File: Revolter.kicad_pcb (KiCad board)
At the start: 2 copper layers, 100 x 100 mm, 179 parts, among them IC1 LM5017, IC2 AP65111, IC3 INA181A1, IC4 INA181A1, P1 USB_OTG, P10 AUX, P2 CAN, P3 IN+, P4 IN-, P5 MOTOR3, P6 MOTOR2, P7 MOTOR1, P8 SWD, P9 Motor, Q1 ZXTC2045E6, Q10 ZXTC2045E6, Q13 IRFB4110, Q14 IRFB4110, Q15 IRFB4110, Q16 IRFB4110, Q19 IRFB4110, Q2 ZXTC2045E6, Q20 IRFB4110, Q21 IRFB4110, Q22 IRFB4110, Q3 IRFB4110, Q4 IRFB4110, Q5 ZXTC2045E6, Q6 ZXTC2045E6, Q7 IRFB4110, Q8 IRFB4110, Q9 ZXTC2045E6, U1 STM32F40X_LQFP64, U2 IR2110S, U3 IR2110S, U4 IR2110S, U5 PCA82C251, U6 7805_SO8, X1 8MHz 10ppm

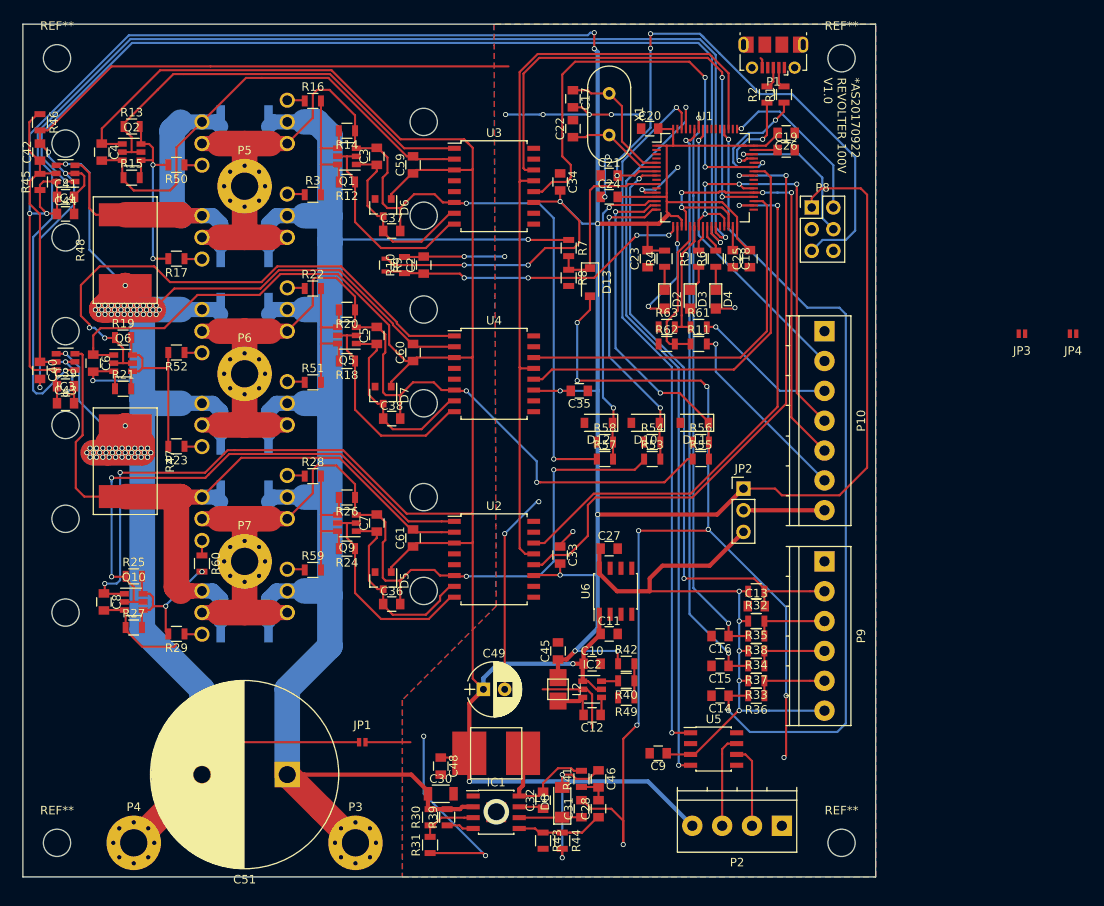
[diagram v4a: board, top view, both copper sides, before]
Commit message: - basis commit for V1.1 - did an great overhaul of high current paths - fixed wrong 3V3 reg pin out - blew the IO connector up to 8 pins (turns out 7pin is rare) - changed shunt to 2512 - changed hf caps to double 1210 - two input caps - pin outs for all IO on silk screen - spread the references so you can actually read them - connected the Hall/Temp pull-ups to 3V3 instead of 5V - changed vias to 0.6/0.3mm - changed text to V1.1
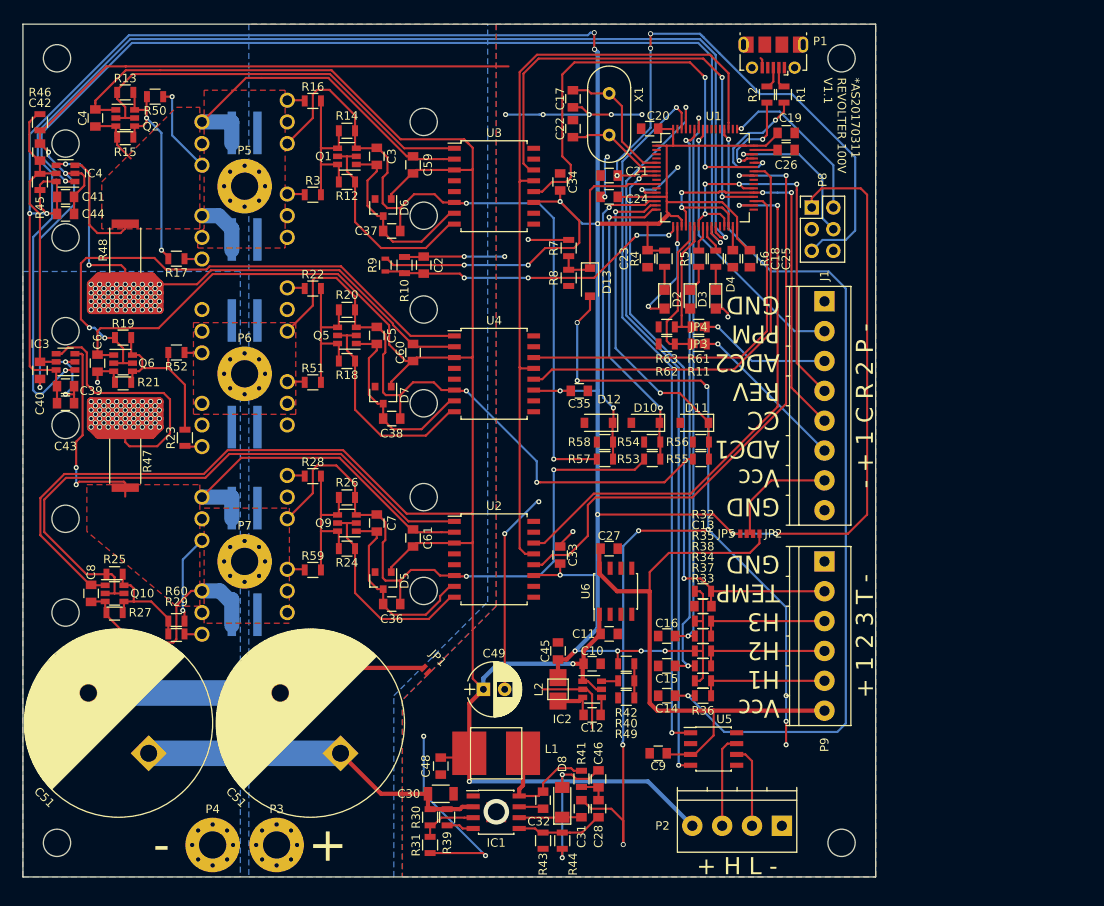
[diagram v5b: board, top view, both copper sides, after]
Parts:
- removed P10: AUX, Connectors_Terminal_Blocks:TerminalBlock_Pheonix_PT-3.5mm_7pol
- added C1: 2u2 250V, Capacitors_SMD:C_1210, B.Cu at (85.0, 65.0)
- added C29: 2u2 250V, Capacitors_SMD:C_1210, B.Cu at (85.0, 55.0)
- added C47: 2u2 250V, Capacitors_SMD:C_1210, B.Cu at (85.0, 87.0)
- added C50: 2u2 250V, Capacitors_SMD:C_1210, B.Cu at (85.0, 77.0)
- added C51: 1mF 100V, alexmod:C_Radial_D22_P10, F.Cu at (73.8, 126.5)
- added C53: 2u2 250V, Capacitors_SMD:C_1210, B.Cu at (85.0, 99.0)
- added C62: 2u2 250V, Capacitors_SMD:C_1210, B.Cu at (85.0, 109.0)
- added J1: IO, Connectors_Terminal_Blocks:TerminalBlock_Pheonix_PT-3.5mm_8pol, F.Cu at (153.0, 73.5)
- added JP5: opt., alexmod:Jumper_2, F.Cu at (143.5, 100.8)
- C52, C54, C55, C56, C57, C58: footprint Capacitors_SMD:C_2220 -> Capacitors_SMD:C_1210
- JP2: value Vcc select -> opt.; footprint Pin_Headers:Pin_Header_Straight_1x03_Pitch2.54mm -> alexmod:Jumper_2
- R47, R48: footprint alexmod:CSS3920 -> Resistors_SMD:R_2512
- moved JP4 43.9 mm to (138.2, 76.5), turned to 180 degrees
- moved JP3 37.9 mm to (138.2, 78.5), turned to 180 degrees
- moved JP1 11.3 mm to (106.2, 116.8), turned to 135 degrees
- moved P3 9.25 mm to (88.8, 137.2)
- moved P4 9.25 mm to (81.2, 137.2)
- moved R50 8.38 mm to (74.5, 49.5)
- moved R60 7.39 mm to (77.0, 111.0), turned to 180 degrees
- moved C51 6.73 mm to (96.2, 126.5), turned to 135 degrees
- moved C13 6.25 mm to (138.8, 109.2)
- moved C14 6.25 mm to (134.5, 119.8)
- moved C15 6.25 mm to (134.5, 116.2)
- moved C16 6.25 mm to (134.5, 112.8)
- moved R32 6.25 mm to (138.8, 107.5)
- moved R33 6.25 mm to (138.8, 118.0)
- moved R34 6.25 mm to (138.8, 114.5)
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- renumbered REF** to ?
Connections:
- JP2 pad 1: +3V3 -> +5V
- R32 pad 2: +5V -> +3V3
- R33 pad 2: +5V -> +3V3
- R34 pad 2: +5V -> +3V3
- R35 pad 2: +5V -> +3V3
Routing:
- net +BATT: track 192.2 -> 46.9 mm
- net GNDPWR: track 233.3 -> 345.1 mm, vias 65 -> 123
- net /Mosfet driver/H1_VS: track 128.2 -> 85.2 mm
- net /Mosfet driver/H3_VS: track 116.6 -> 73.6 mm
- net /Mosfet driver/H2_VS: track 117.8 -> 74.8 mm
- net /Mosfet driver/H1_LOW: track 100.2 -> 68.9 mm
- net +3V3: track 399.0 -> 427.3 mm, vias 13 -> 17
- net Net-(Q22-Pad1): track 1.76 -> 10.5 mm, vias 0 -> 1
- net Net-(Q8-Pad1): track 2.07 -> 10.5 mm, vias 0 -> 1
- net /Mosfet driver/M_L3: track 63.5 -> 71.9 mm, vias 2 -> 0
- net /Mosfet driver/H3_LOW: track 100.6 -> 93.0 mm, vias 0 -> 2
- net GND: track 363.4 -> 356.3 mm, vias 34 -> 35
- net /Filters/HALL3_IN: track 8.80 -> 15.1 mm
- net /Filters/HALL2_IN: track 8.80 -> 15.1 mm
- net /Filters/HALL1_IN: track 8.80 -> 15.1 mm
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- added copper zone on B.Cu, net +BATT
- added copper zone on F.Cu, net /Mosfet driver/H1_LOW
- added copper zone on F.Cu, net /Mosfet driver/H1_VS
- added copper zone on F.Cu, net /Mosfet driver/H2_VS
- added copper zone on F.Cu, net /Mosfet driver/H3_LOW
- added copper zone on F.Cu, net /Mosfet driver/H3_VS
- added copper zone on B.Cu, net GNDPWR
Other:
- net class Default: via_drill 0.4 -> 0.3
- rule pad_to_mask_clearance: 0.05 -> 0.1
- rule via_min_size: 0.4 -> 0.6
- board text added: "*AS20170311 REVOLTER 100V V1.1"
- board text added: "+"
- board text added: "+ 1 2 3 T -"
- board text added: "+ H L -"
- board text added: "-"
- board text added: "- + 1 C R 2 P -"
- board text added: "GND Vcc ADC1 CC REV ADC2 PPM GND"
- board text added: "Vcc H1 H2 H3 TEMP GND"
- board text removed: "*AS20170922 REVOLTER 100V V1.0"

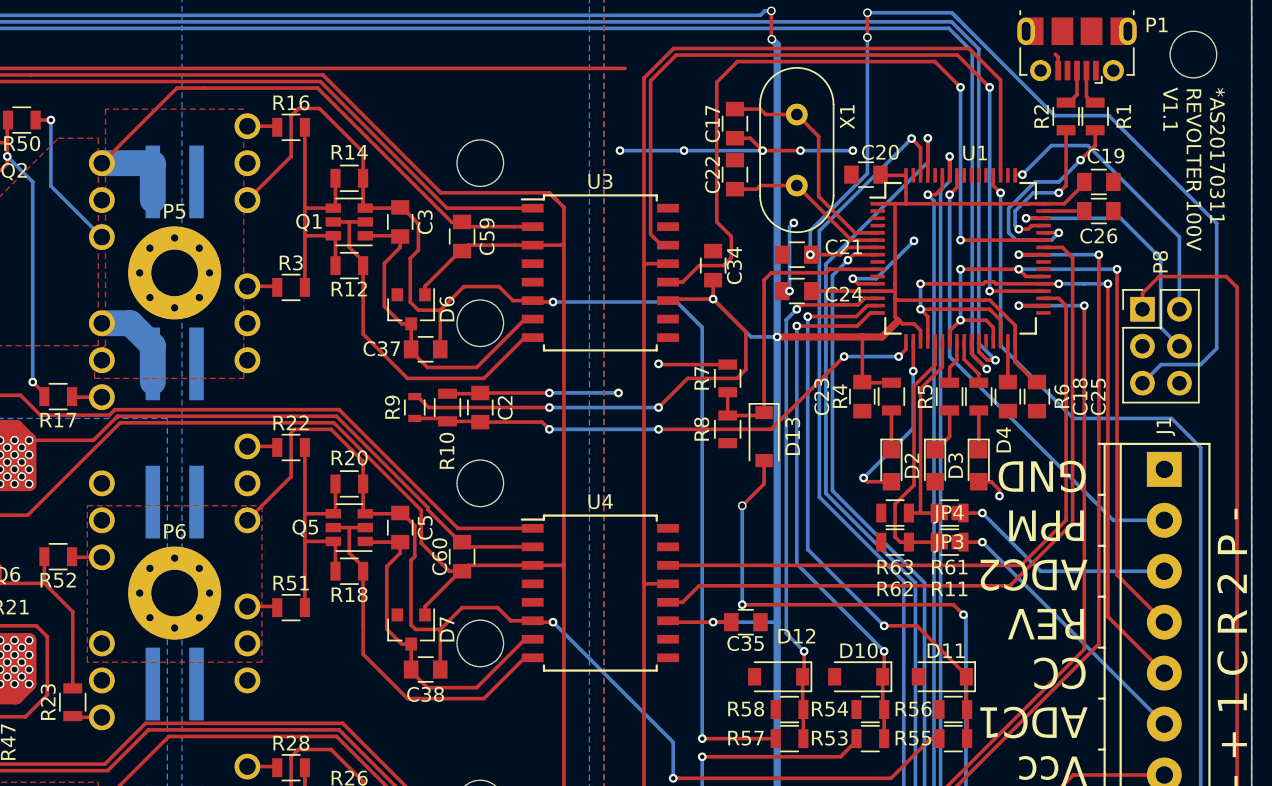
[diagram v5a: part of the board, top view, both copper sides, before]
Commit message: - fixed a issue with the central motor phase copper lane - changed text to V1.2
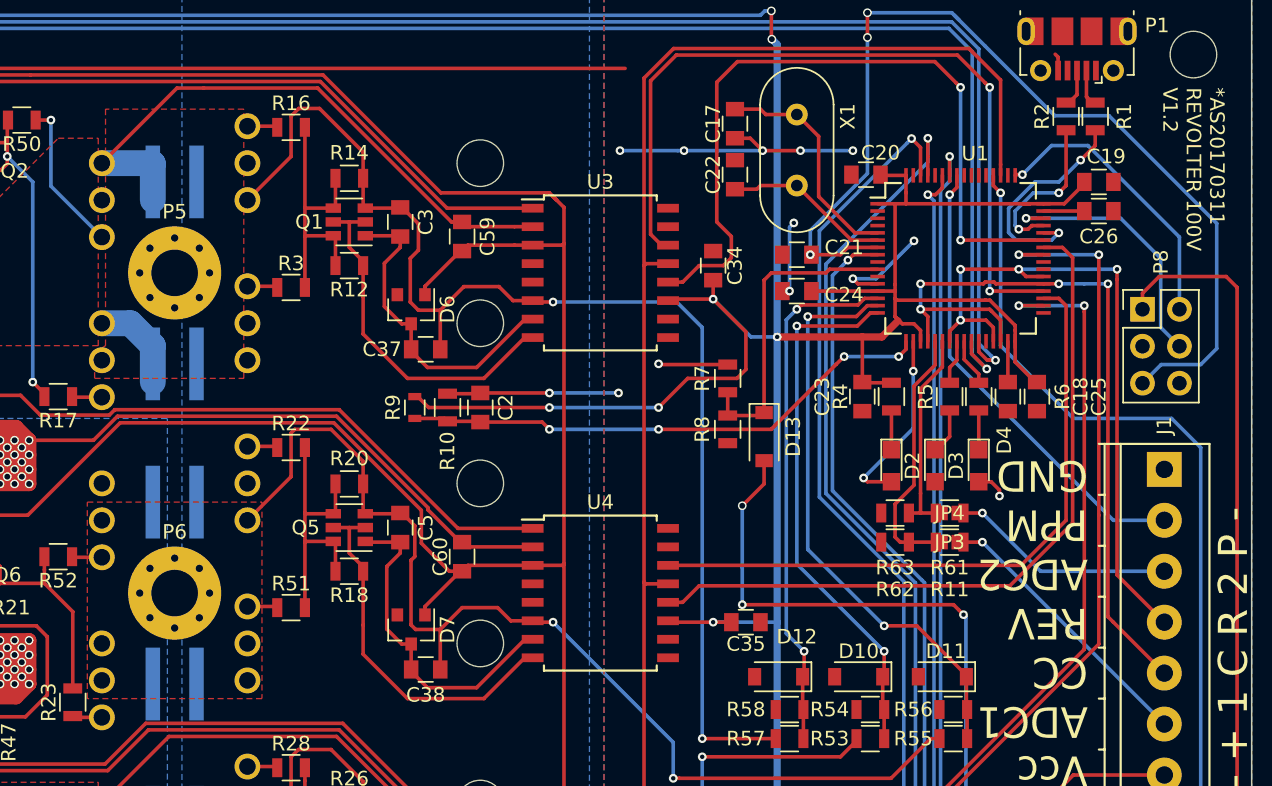
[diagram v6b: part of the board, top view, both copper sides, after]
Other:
- board text added: "*AS20170311 REVOLTER 100V V1.2"
- board text removed: "*AS20170311 REVOLTER 100V V1.1"
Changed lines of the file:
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@@
   (general
     (links 427)
-    (no_connects 22)
+    (no_connects 20)
     (area 50.371429 39.325 167.628572 142.525)
     (thickness 1.6)
@@
     (effects (font (size 2.1 2) (thickness 0.3)) (justify left))
   )
-  (gr_text "*AS20170311\nREVOLTER 100V\nV1.1" (at 155 47.25 270) (layer F.SilkS)
+  (gr_text "*AS20170311\nREVOLTER 100V\nV1.2" (at 155 47.25 270) (layer F.SilkS)
     (effects (font (size 1 1) (thickness 0.15)) (justify left))
   )
@@
     (polygon
       (pts
-        (xy 79 76) (xy 91 76) (xy 91 86.75) (xy 79 86.75)
+        (xy 79 75.75) (xy 91 75.75) (xy 91 89.25) (xy 79 89.25)
       )
     )

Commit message: - changed dividers to 100k vs 3k3
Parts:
- R53, R55, R57: value 220k -> 100k
- R54, R56, R58: value 12k -> 3k3
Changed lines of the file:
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@@
     (links 427)
     (no_connects 20)
-    (area 50.371429 39.325 167.628572 142.525)
+    (area 58.949999 40.949999 159.050001 141.050001)
     (thickness 1.6)
     (drawings 12)
@@
       (effects (font (size 1 1) (thickness 0.15)))
     )
-    (fp_text value 12k (at 0 1.75) (layer F.Fab)
+    (fp_text value 3k3 (at 0 1.75) (layer F.Fab)
       (effects (font (size 1 1) (thickness 0.15)))
     )
@@
       (effects (font (size 1 1) (thickness 0.15)))
     )
-    (fp_text value 220k (at 0 1.75) (layer F.Fab)
+    (fp_text value 100k (at 0 1.75) (layer F.Fab)
       (effects (font (size 1 1) (thickness 0.15)))
     )
@@
       (effects (font (size 1 1) (thickness 0.15)))
     )
-    (fp_text value 12k (at 0 1.75) (layer F.Fab)
+    (fp_text value 3k3 (at 0 1.75) (layer F.Fab)
       (effects (font (size 1 1) (thickness 0.15)))
     )
@@
       (effects (font (size 1 1) (thickness 0.15)))
     )
-    (fp_text value 220k (at 0 1.75) (layer F.Fab)
+    (fp_text value 100k (at 0 1.75) (layer F.Fab)
       (effects (font (size 1 1) (thickness 0.15)))
     )
@@
       (effects (font (size 1 1) (thickness 0.15)))
     )
-    (fp_text value 12k (at 0 1.75) (layer F.Fab)
+    (fp_text value 3k3 (at 0 1.75) (layer F.Fab)
       (effects (font (size 1 1) (thickness 0.15)))
     )
@@
       (effects (font (size 1 1) (thickness 0.15)))
     )
-    (fp_text value 220k (at 0 1.75) (layer F.Fab)
-      (effects (font (size 1 1) (thickness 0.15)))
-    )
+    (fp_text value 100k (at 0 1.75) (layer F.Fab)
+      (effects (font (size 1 1) (thickness 0.15)))
+    )

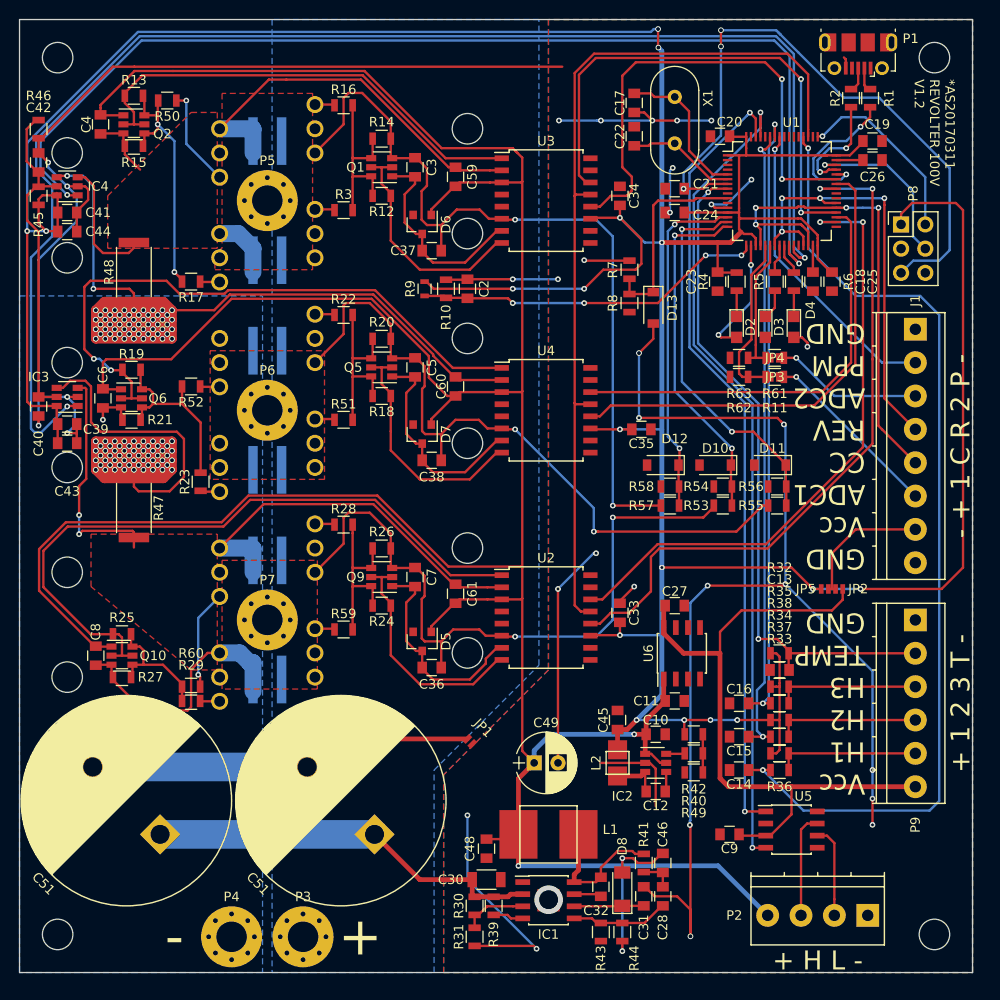
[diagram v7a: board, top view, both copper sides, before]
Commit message: - updated project to 5.0.0 - added some more ignores
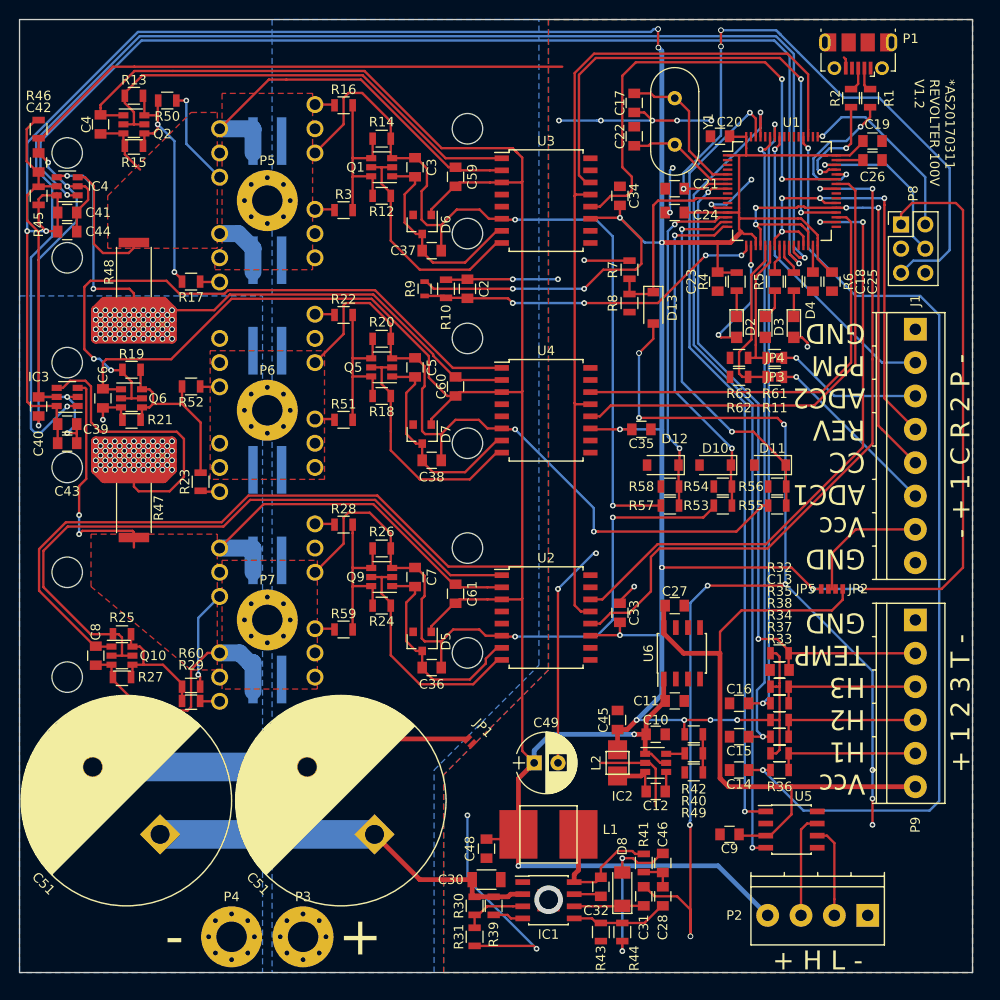
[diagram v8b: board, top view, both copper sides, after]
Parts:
- removed ? (x4): MountingHole_3.2mm_M3_DIN965, Mounting_Holes:MountingHole_3.2mm_M3_DIN965
- removed X1: 8MHz 10ppm, Crystals:Crystal_HC49-U_Vertical
- added Y1: Crystal, Crystals:Crystal_HC49-U_Vertical, F.Cu at (127.8, 49.2)
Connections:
- P1 pad 1: (no net) -> Net-(P1-Pad1)
- P1 pad 4: (no net) -> Net-(P1-Pad4)
- P8 pad 6: (no net) -> Net-(P8-Pad6)
- U1 pad 11: (no net) -> Net-(U1-Pad11)
- U1 pad 2: (no net) -> Net-(U1-Pad2)
- U1 pad 28: (no net) -> Net-(U1-Pad28)
- U1 pad 3: (no net) -> Net-(U1-Pad3)
- U1 pad 33: (no net) -> /MCU/DC_CAL
- U1 pad 39: (no net) -> Net-(U1-Pad39)
- U1 pad 4: (no net) -> Net-(U1-Pad4)
- U1 pad 40: (no net) -> Net-(U1-Pad40)
- U1 pad 50: (no net) -> Net-(U1-Pad50)
- U1 pad 53: (no net) -> /MCU/FAULT
- U1 pad 54: (no net) -> Net-(U1-Pad54)
- U1 pad 55: (no net) -> Net-(U1-Pad55)
- U1 pad 56: (no net) -> Net-(U1-Pad56)
- U1 pad 9: (no net) -> Net-(U1-Pad9)
- U5 pad 5: (no net) -> Net-(U5-Pad5)
- U5 pad 8: (no net) -> Net-(U5-Pad8)
